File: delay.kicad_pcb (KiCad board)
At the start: 2 copper layers, 70 x 90 mm, 56 parts, among them J1 Footswitch_Terminal_01x02, J2 LED_Socket_01x02, J3 Footswitch_Terminal_Signal_01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, J4 Power_Supply_Terminal_01x02, J5 IO_Ground_Terminal_01x02, U1 L7805, U2 TL072, U3 PT2399

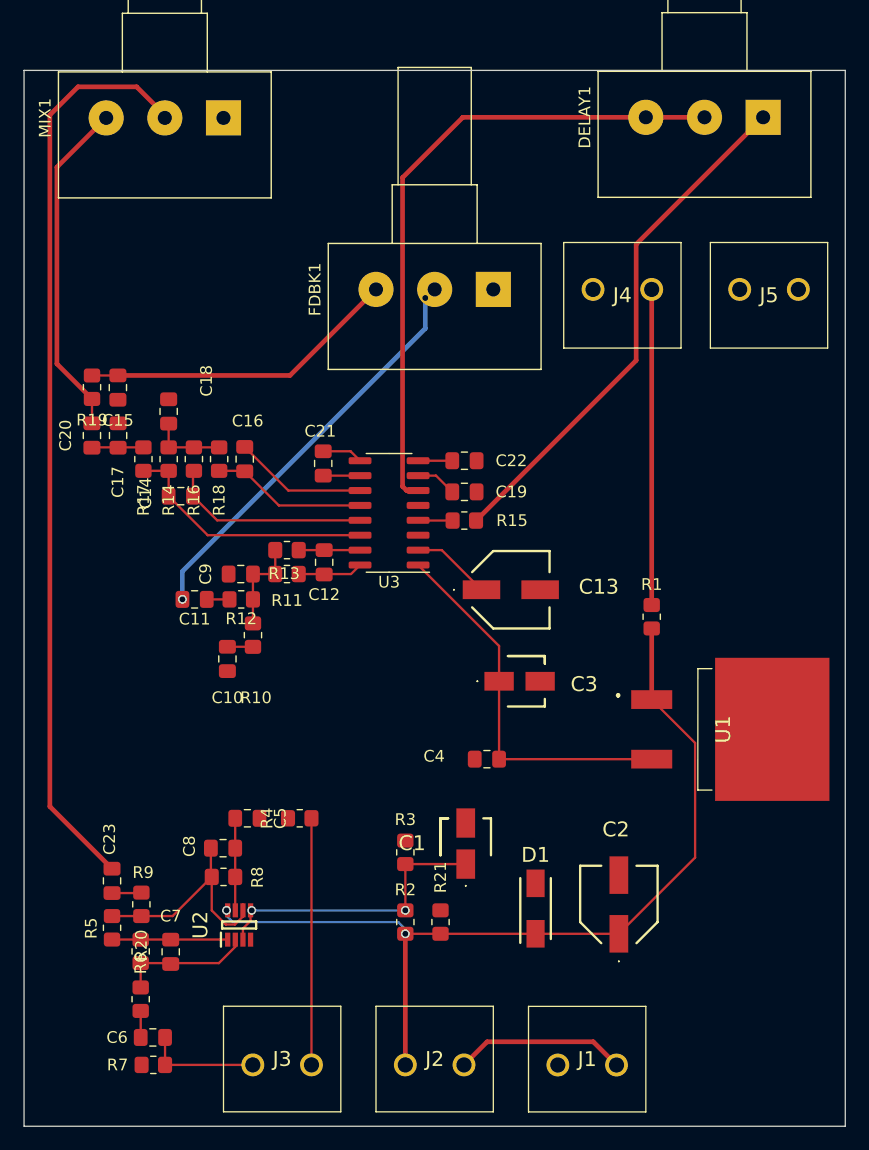
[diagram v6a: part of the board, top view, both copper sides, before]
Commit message: connect mass and reorganise labels
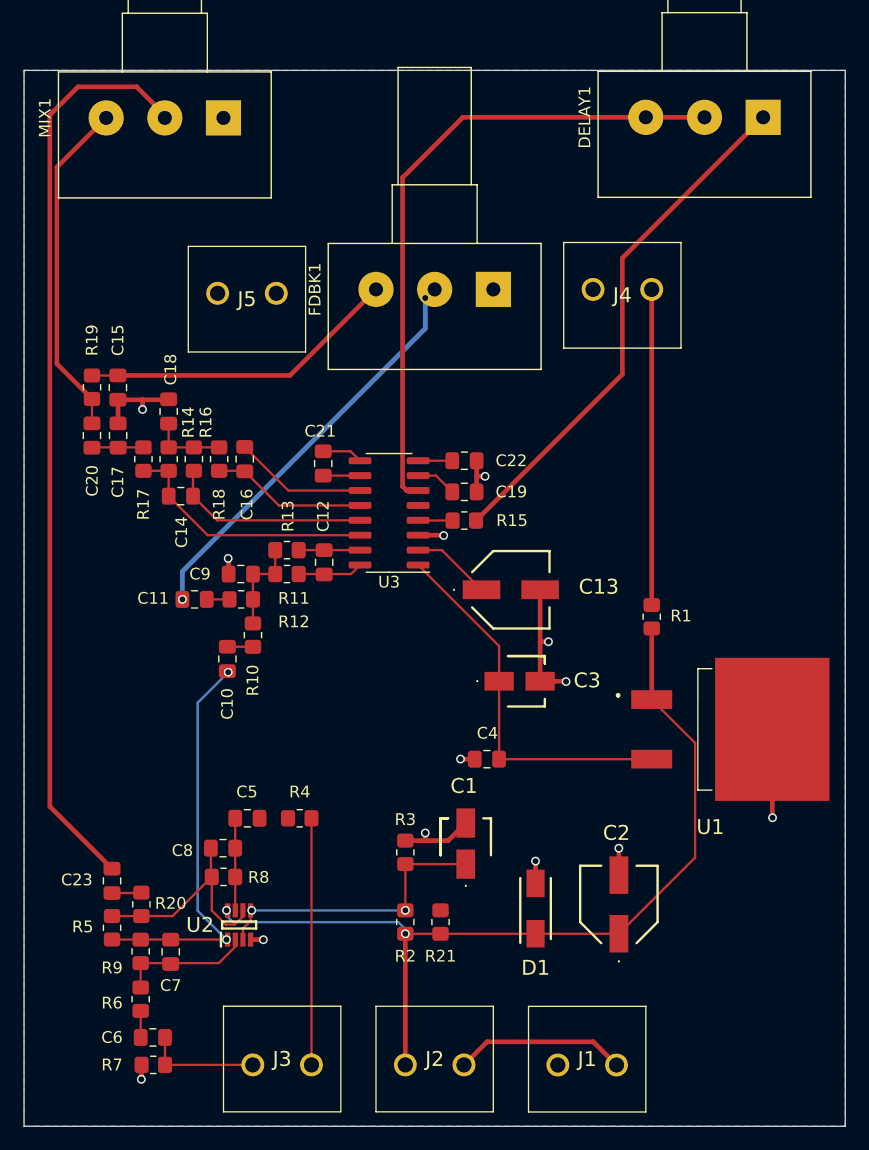
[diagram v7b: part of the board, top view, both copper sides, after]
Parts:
- moved J5 44.5 mm to (136.5, 69.0)
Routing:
- net 0: track 0.00 -> 46.5 mm, vias 0 -> 13
- net /SIGNAL_CLEAN: track 9.86 -> 34.9 mm, vias 0 -> 2
- added copper zone on B.Cu, net 0
